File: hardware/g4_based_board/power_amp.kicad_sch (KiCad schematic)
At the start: 9 parts, among them J5 Screw_Terminal_01x03, Q5 NMOS

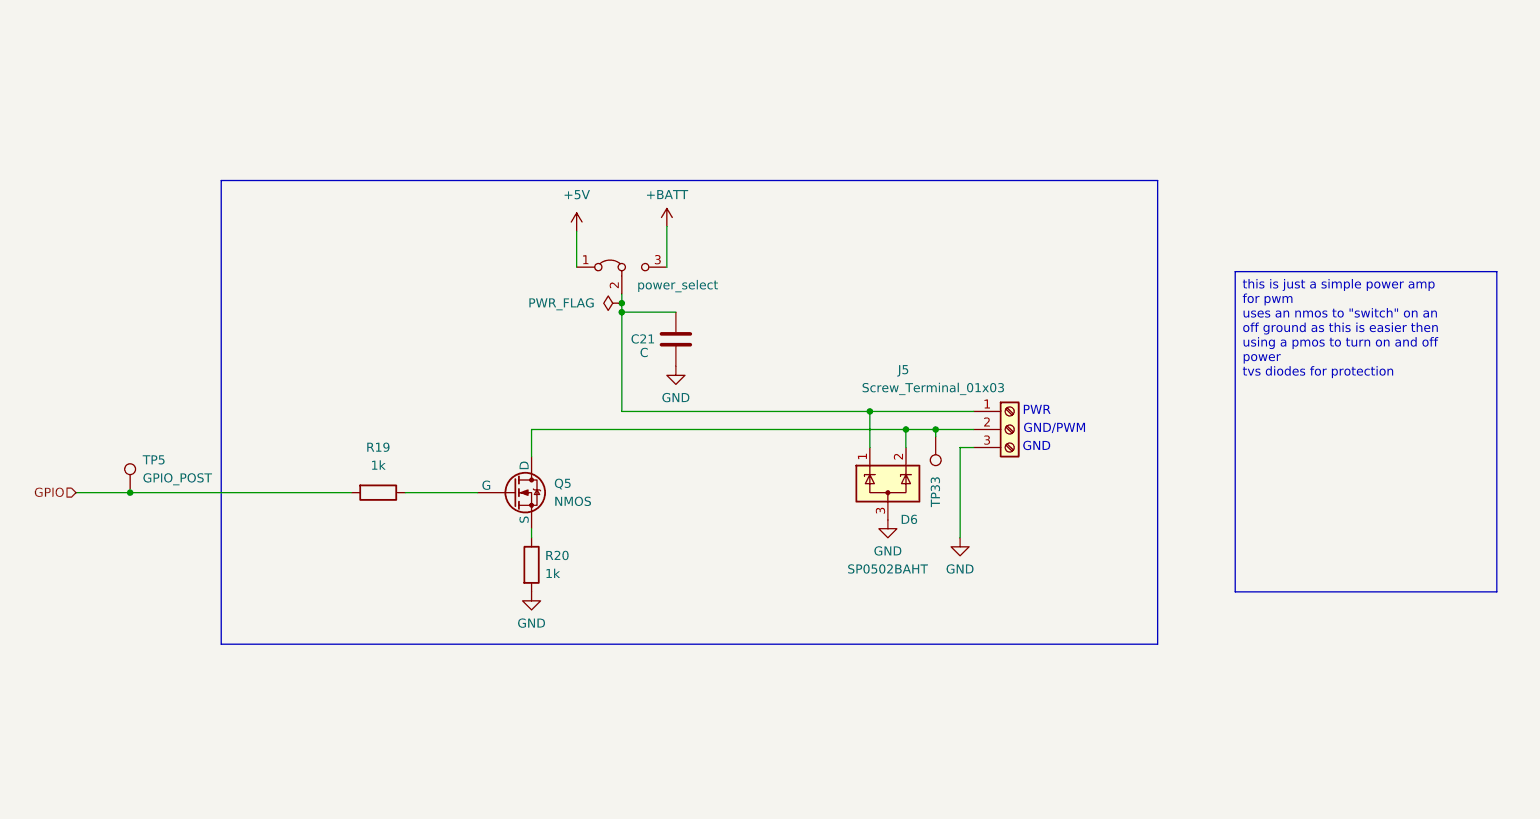
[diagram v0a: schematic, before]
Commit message: changed to high side pmos driver
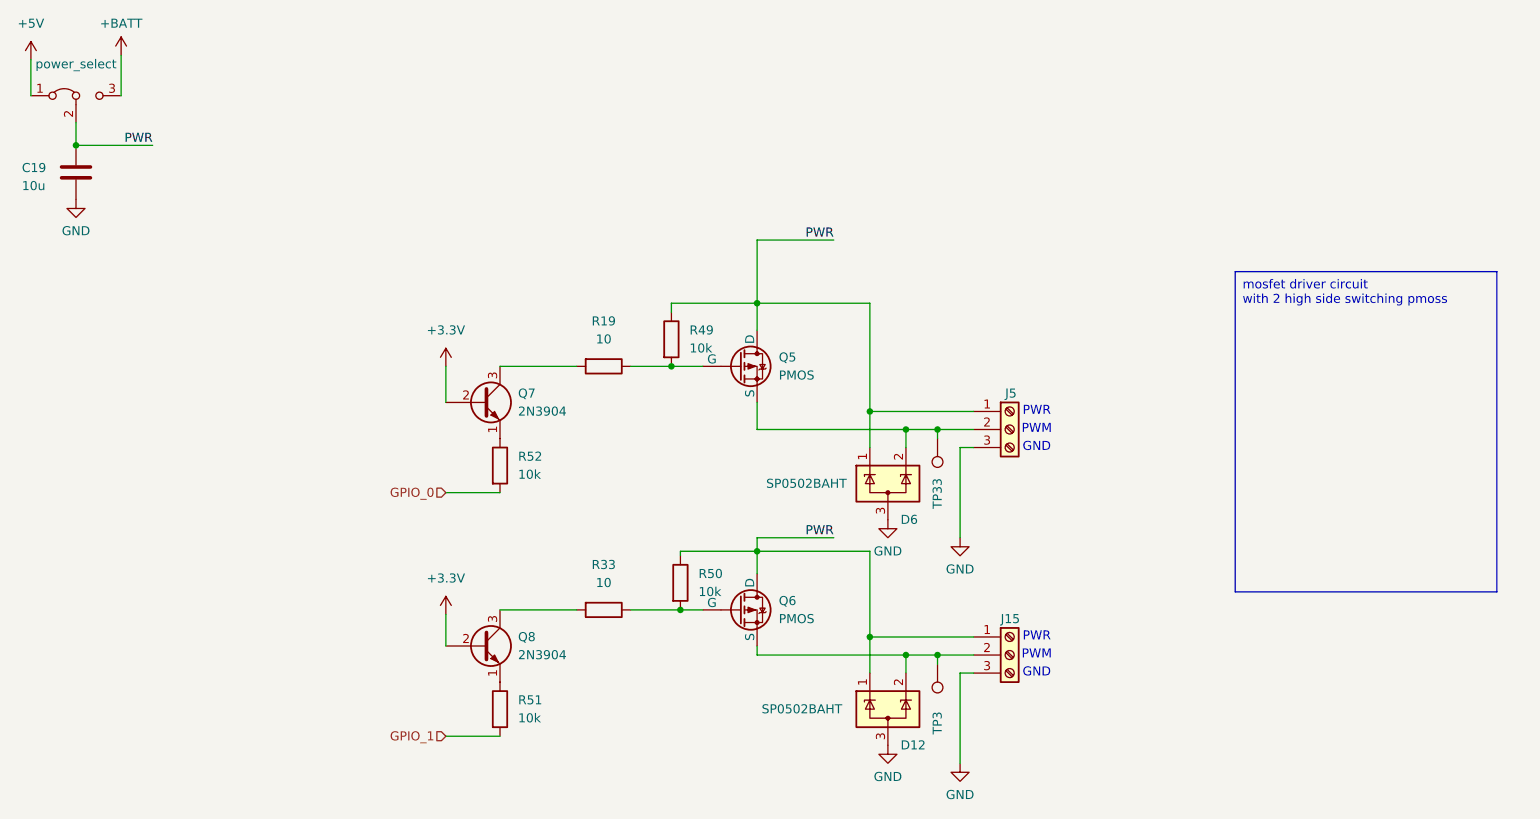
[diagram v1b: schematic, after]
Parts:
- removed C21: C, Capacitor_SMD:C_0603_1608Metric_Pad1.08x0.95mm_HandSolder, symbol Device:C
- removed JP3: power_select, Connector_PinHeader_2.54mm:PinHeader_1x03_P2.54mm_Vertical, symbol Jumper:Jumper_3_Bridged12
- removed Q5: NMOS, Package_TO_SOT_SMD:SOT-23-3, symbol Simulation_SPICE:NMOS
- removed R20: 1k, Resistor_SMD:R_0603_1608Metric_Pad0.98x0.95mm_HandSolder, symbol Device:R
- removed TP5: GPIO_POST, TestPoint:TestPoint_Keystone_5019_Minature, symbol Connector:TestPoint
- added C19: 10u, Capacitor_SMD:C_0603_1608Metric_Pad1.08x0.95mm_HandSolder, symbol Device:C
- added D12: SP0502BAHT, Package_TO_SOT_SMD:SOT-23, symbol Power_Protection:SP0502BAHT
- added J15: Screw_Terminal_01x03, TerminalBlock:TerminalBlock_Altech_AK300-3_P5.00mm, symbol Connector:Screw_Terminal_01x03
- added JP6: power_select, Connector_PinHeader_2.54mm:PinHeader_1x03_P2.54mm_Vertical, symbol Jumper:Jumper_3_Bridged12
- added Q5, Q6: PMOS, Package_TO_SOT_THT:TO-247-3_Vertical, symbol Simulation_SPICE:PMOS
- added Q7, Q8: 2N3904, Package_TO_SOT_THT:TO-92_Inline, symbol Transistor_BJT:2N3904
- added R33: 10, Resistor_SMD:R_0603_1608Metric_Pad0.98x0.95mm_HandSolder, symbol Device:R
- added R49, R50, R51, R52: 10k, Resistor_SMD:R_0603_1608Metric_Pad0.98x0.95mm_HandSolder, symbol Device:R
- added TP3: GPIO_INPUT_PRE, TestPoint:TestPoint_Keystone_5019_Minature, symbol Connector:TestPoint
- R19: value 1k -> 10
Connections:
- net +5V: now also JP6.1 (A)
- net +BATT: now also JP6.3 (B)
- net GND: now also C19.2, D12.3 (A), J15.3 (Pin_3)
- net PWR: now reaches D6.1 (K), J5.1 (Pin_1)
- net PWR: now also C19.1, D12.1 (K), J15.1 (Pin_1), JP6.2 (C), Q5.1 (D), Q6.1 (D), R49.1, R50.1
- net at D6.2 (K), J5.2 (Pin_2), TP33.1: now also Q5.3 (S)
- net at R19.1: now also Q5.2 (G), R49.2
- net GPIO: no longer names the net of R19.2
- net GPIO: now also Q7.3 (C)
- new net: D12.2 (K), J15.2 (Pin_2), Q6.3 (S), TP3.1
- new net: Q8.1 (E), R51.1
- new net: Q7.1 (E), R52.1
- new net: Q6.2 (G), R33.1, R50.2
- new net: Q8.3 (C), R33.2
- new net +3.3V: Q7.2 (B), Q8.2 (B)
- new net GPIO_0: R52.2
- new net GPIO_1: R51.2
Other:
- note added: "PWM"
- note removed: "GND/PWM"
- moved on the sheet: R19
